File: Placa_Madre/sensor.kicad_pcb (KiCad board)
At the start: 2 copper layers, 10 parts, among them J1 Screw_Terminal_01x02, J2 Screw_Terminal_01x04, J3 Screw_Terminal_01x04, J4 Screw_Terminal_01x04, J5 Screw_Terminal_01x02, J6 Screw_Terminal_01x02, U1 RASPBERRY_PI_4B_4GB, U2 TMC2208_SILENTSTEPSTICK, U3 TMC2208_SILENTSTEPSTICK, U4 TMC2208_SILENTSTEPSTICK

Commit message: Add files via upload
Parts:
- J4: moved to B.Cu
- moved J1 78.1 mm to (58.4, 107.8), turned to 90 degrees
- moved J5 56.1 mm to (90.5, 110.5), turned to 90 degrees
- moved J6 43.7 mm to (120.0, 107.5), turned to 180 degrees
- moved J4 41.0 mm to (118.5, 99.5), turned to 90 degrees
- moved U4 38.6 mm to (133.3, 95.4)
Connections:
- U1 pad 11: unconnected-(U1-GPIO17/GPIO_GEN0-Pad11) -> DIR3
- U1 pad 12: STEP3 -> STEP2
- U1 pad 16: unconnected-(U1-GPIO23/GPIO_GEN4-Pad16) -> DIR2
- U1 pad 33: STEP2 -> STEP3
- U1 pad 35: DIR2 -> unconnected-(U1-GPIO19-Pad35)
- U1 pad 36: DIR -> DIR1
- U1 pad 38: DIR3 -> unconnected-(U1-GPIO20-Pad38)
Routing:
- net GND: track 0.00 -> 322.4 mm
- net VIO: track 0.00 -> 97.9 mm
- net STEP3: track 0.00 -> 93.2 mm
- net DIR3: track 0.00 -> 53.9 mm
- net STEP1: track 0.00 -> 20.8 mm
- net STEP2: track 0.00 -> 20.3 mm
- net VIO2: track 0.00 -> 18.1 mm
- net DIR1: track 0.00 -> 16.2 mm
- net VM2: track 0.00 -> 15.9 mm
- net DIR2: track 0.00 -> 15.7 mm
- net VM1: track 0.00 -> 13.7 mm
- net VM3: track 0.00 -> 10.3 mm
- net Net-(J3-Pin_4): track 0.00 -> 9.65 mm
- net Net-(J3-Pin_3): track 0.00 -> 9.65 mm
- net Net-(J3-Pin_2): track 0.00 -> 9.65 mm
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
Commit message: Add files via upload
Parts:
- added J7: Screw_Terminal_01x02, TerminalBlock_MetzConnect:TerminalBlock_MetzConnect_360272_1x01_Horizontal_ScrewM2.6, F.Cu at (67.5, 110.0)
- added J8: Screw_Terminal_01x02, TerminalBlock_MetzConnect:TerminalBlock_MetzConnect_360272_1x01_Horizontal_ScrewM2.6, F.Cu at (135.0, 107.5)
- added J9: Screw_Terminal_01x02, TerminalBlock_MetzConnect:TerminalBlock_MetzConnect_360272_1x01_Horizontal_ScrewM2.6, F.Cu at (137.5, 103.0)
- added REF**: TerminalBlock_MetzConnect_360272_1x01_Horizontal_ScrewM2.6, TerminalBlock_MetzConnect:TerminalBlock_MetzConnect_360272_1x01_Horizontal_ScrewM2.6, F.Cu at (107.5, 67.5)
- added REF**: TerminalBlock_MetzConnect_360272_1x01_Horizontal_ScrewM2.6, TerminalBlock_MetzConnect:TerminalBlock_MetzConnect_360272_1x01_Horizontal_ScrewM2.6, F.Cu at (107.5, 78.0)
- added REF**: TerminalBlock_MetzConnect_360272_1x01_Horizontal_ScrewM2.6, TerminalBlock_MetzConnect:TerminalBlock_MetzConnect_360272_1x01_Horizontal_ScrewM2.6, F.Cu at (144.5, 77.5)
- added REF**: TerminalBlock_MetzConnect_360272_1x01_Horizontal_ScrewM2.6, TerminalBlock_MetzConnect:TerminalBlock_MetzConnect_360272_1x01_Horizontal_ScrewM2.6, F.Cu at (120.0, 90.0)
- J1, J5, J6: footprint TerminalBlock_Phoenix:TerminalBlock_Phoenix_MPT-0,5-2-2.54_1x02_P2.54mm_Horizontal -> TerminalBlock_MetzConnect:TerminalBlock_MetzConnect_360272_1x01_Horizontal_ScrewM2.6
- J2, J3: value Screw_Terminal_01x04 -> Screw_Terminal_01x02; footprint TerminalBlock_Phoenix:TerminalBlock_Phoenix_MPT-0,5-4-2.54_1x04_P2.54mm_Horizontal -> TerminalBlock_MetzConnect:TerminalBlock_MetzConnect_360272_1x01_Horizontal_ScrewM2.6
- J4: value Screw_Terminal_01x04 -> Screw_Terminal_01x02; footprint TerminalBlock_Phoenix:TerminalBlock_Phoenix_MPT-0,5-4-2.54_1x04_P2.54mm_Horizontal -> TerminalBlock_MetzConnect:TerminalBlock_MetzConnect_360272_1x01_Horizontal_ScrewM2.6; moved to F.Cu
- moved J4 51.1 mm to (67.5, 103.0)
- moved J2 46.0 mm to (105.0, 105.0)
- moved J3 20.7 mm to (105.0, 112.5)
- moved J1 19.8 mm to (74.9, 118.8)
- moved J5 19.8 mm to (107.0, 121.5)
- moved J6 19.8 mm to (136.5, 118.5)
- moved U1 19.8 mm to (112.5, 57.5)
- moved U2 19.8 mm to (91.5, 106.0)
- moved U3 19.8 mm to (121.0, 107.2)
- moved U4 19.8 mm to (149.8, 106.4)
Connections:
- U1 pad 11: DIR3 -> unconnected-(U1-GPIO17/GPIO_GEN0-Pad11)
- U1 pad 12: STEP2 -> STEP3
- U1 pad 16: DIR2 -> unconnected-(U1-GPIO23/GPIO_GEN4-Pad16)
- U1 pad 33: STEP3 -> STEP2
- U1 pad 35: unconnected-(U1-GPIO19-Pad35) -> DIR2
- U1 pad 36: DIR1 -> DIR
- U1 pad 38: unconnected-(U1-GPIO20-Pad38) -> DIR3
- U2 pad JP2_3: Net-(J2-Pin_2) -> Net-(J7-Pin_2)
- U2 pad JP2_4: Net-(J2-Pin_1) -> Net-(J7-Pin_1)
- U2 pad JP2_5: Net-(J2-Pin_3) -> Net-(J4-Pin_1)
- U2 pad JP2_6: Net-(J2-Pin_4) -> Net-(J4-Pin_2)
- U3 pad JP2_5: Net-(J3-Pin_3) -> Net-(J2-Pin_1)
- U3 pad JP2_6: Net-(J3-Pin_4) -> Net-(J2-Pin_2)
- U4 pad JP2_3: Net-(J4-Pin_2) -> Net-(J8-Pin_2)
- U4 pad JP2_4: Net-(J4-Pin_1) -> Net-(J8-Pin_1)
- U4 pad JP2_5: Net-(J4-Pin_3) -> Net-(J9-Pin_1)
- U4 pad JP2_6: Net-(J4-Pin_4) -> Net-(J9-Pin_2)
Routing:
- net Net-(J7-Pin_2): track 0.00 -> 18.4 mm
- net Net-(J7-Pin_1): track 0.00 -> 18.2 mm
- net Net-(J4-Pin_2): track 8.62 -> 18.6 mm
- net GND: track 322.4 -> 312.5 mm
- net Net-(J4-Pin_1): track 8.62 -> 18.4 mm
- net Net-(J3-Pin_4): track 9.65 -> 0.00 mm
- net Net-(J3-Pin_3): track 9.65 -> 0.00 mm
- net Net-(J2-Pin_4): track 9.49 -> 0.00 mm
- net Net-(J2-Pin_3): track 9.49 -> 0.00 mm
- net Net-(J8-Pin_2): track 0.00 -> 9.05 mm
- net Net-(J8-Pin_1): track 0.00 -> 8.99 mm
- net Net-(J4-Pin_4): track 8.62 -> 0.00 mm
- net Net-(J4-Pin_3): track 8.62 -> 0.00 mm
- net Net-(J9-Pin_2): track 0.00 -> 7.49 mm
- net Net-(J9-Pin_1): track 0.00 -> 7.30 mm
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- added copper zone on B.Cu, net GND

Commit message: Add files via upload
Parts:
- removed the REF** at (107.5, 67.5)
- removed the REF** at (144.5, 77.5)
- moved REF** 16.2 mm to (123.5, 75.5), turned to 0 degrees
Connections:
- REF** pad 1: (no net) -> VIO (x2)
- U1 pad 13: unconnected-(U1-GPIO27/GPIO_GEN2-Pad13) -> STEP3
- U4 pad JP2_7: VIO2 -> VIO
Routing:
- net VIO: track 104.8 -> 144.5 mm
- net VIO2: track 18.1 -> 0.00 mm
- net STEP3: track 93.2 -> 80.5 mm
- net GND: track 312.5 -> 305.8 mm
- net DIR3: track 53.8 -> 60.1 mm
- net STEP2: track 25.2 -> 21.4 mm
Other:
- board outline added: 107 x 107.5 mm

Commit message: arreglando el pcb
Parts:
- removed J1, J2, J3, J4, J5, J6, J7, J8, J9: Screw_Terminal_01x02, TerminalBlock_MetzConnect:TerminalBlock_MetzConnect_360272_1x01_Horizontal_ScrewM2.6
- removed the REF** at (123.5, 75.5)
- removed the REF** at (120.0, 90.0)
- added REF**: TerminalBlock_MetzConnect_360291_1x01_Horizontal_ScrewM3.0_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, TerminalBlock_MetzConnect:TerminalBlock_MetzConnect_360291_1x01_Horizontal_ScrewM3.0_Boxed, F.Cu at (137.5, 107.5)
- added REF**: TerminalBlock_MetzConnect_360291_1x01_Horizontal_ScrewM3.0_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, TerminalBlock_MetzConnect:TerminalBlock_MetzConnect_360291_1x01_Horizontal_ScrewM3.0_Boxed, F.Cu at (140.0, 122.5)
- added REF**: TerminalBlock_MetzConnect_360291_1x01_Horizontal_ScrewM3.0_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, TerminalBlock_MetzConnect:TerminalBlock_MetzConnect_360291_1x01_Horizontal_ScrewM3.0_Boxed, F.Cu at (115.0, 125.0)
- added REF**: TerminalBlock_MetzConnect_360291_1x01_Horizontal_ScrewM3.0_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, TerminalBlock_MetzConnect:TerminalBlock_MetzConnect_360291_1x01_Horizontal_ScrewM3.0_Boxed, F.Cu at (105.0, 122.5)
- added REF**: TerminalBlock_MetzConnect_360291_1x01_Horizontal_ScrewM3.0_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, TerminalBlock_MetzConnect:TerminalBlock_MetzConnect_360291_1x01_Horizontal_ScrewM3.0_Boxed, F.Cu at (67.5, 115.0)
- added REF**: TerminalBlock_MetzConnect_360291_1x01_Horizontal_ScrewM3.0_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, TerminalBlock_MetzConnect:TerminalBlock_MetzConnect_360291_1x01_Horizontal_ScrewM3.0_Boxed, F.Cu at (141.5, 90.0)
- added REF**: TerminalBlock_MetzConnect_360291_1x01_Horizontal_ScrewM3.0_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, TerminalBlock_MetzConnect:TerminalBlock_MetzConnect_360291_1x01_Horizontal_ScrewM3.0_Boxed, F.Cu at (107.5, 107.5)
- added REF**: TerminalBlock_MetzConnect_360291_1x01_Horizontal_ScrewM3.0_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, TerminalBlock_MetzConnect:TerminalBlock_MetzConnect_360291_1x01_Horizontal_ScrewM3.0_Boxed, F.Cu at (125.0, 72.5)
- added REF**: TerminalBlock_MetzConnect_360291_1x01_Horizontal_ScrewM3.0_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, TerminalBlock_MetzConnect:TerminalBlock_MetzConnect_360291_1x01_Horizontal_ScrewM3.0_Boxed, F.Cu at (67.5, 102.5)
- added REF**: TerminalBlock_MetzConnect_360291_1x01_Horizontal_ScrewM3.0_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, TerminalBlock_MetzConnect:TerminalBlock_MetzConnect_360291_1x01_Horizontal_ScrewM3.0_Boxed, F.Cu at (122.5, 90.0)
- added REF**: TerminalBlock_MetzConnect_360291_1x01_Horizontal_ScrewM3.0_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, TerminalBlock_MetzConnect:TerminalBlock_MetzConnect_360291_1x01_Horizontal_ScrewM3.0_Boxed, F.Cu at (85.0, 125.0)
- added REF**: TerminalBlock_MetzConnect_360291_1x01_Horizontal_ScrewM3.0_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, TerminalBlock_MetzConnect:TerminalBlock_MetzConnect_360291_1x01_Horizontal_ScrewM3.0_Boxed, F.Cu at (155.0, 121.0)
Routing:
- net GND: track 305.8 -> 52.2 mm
- net VIO: track 144.5 -> 132.9 mm
- net VM2: track 15.9 -> 5.06 mm
- net Net-(J3-Pin_1): track 10.1 -> 19.7 mm
- net Net-(J8-Pin_1): track 8.99 -> 17.9 mm
- net unconnected-(U1-GPIO14/TXD0-Pad8): track 0.00 -> 7.76 mm
- net VM1: track 13.7 -> 6.17 mm
- net unconnected-(U1-GPIO15/RXD0-Pad10): track 0.00 -> 7.16 mm
- net Net-(J3-Pin_2): track 10.3 -> 15.5 mm
- net Net-(J9-Pin_2): track 7.49 -> 12.5 mm
- net Net-(J8-Pin_2): track 9.05 -> 13.7 mm
- net VM3: track 10.3 -> 13.9 mm
- net Net-(J2-Pin_2): track 10.2 -> 12.9 mm
- net Net-(J2-Pin_1): track 10.0 -> 7.80 mm
- net Net-(J7-Pin_2): track 18.4 -> 19.8 mm
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
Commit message: Correjir PPCB
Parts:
- moved REF** 21.7 mm to (99.0, 127.5)
- moved REF** 20.3 mm to (134.0, 127.5)
- moved REF** 7.91 mm to (122.5, 127.5), turned to 180 degrees
- moved REF** 7.07 mm to (145.0, 127.5)
- moved REF** 7.07 mm to (110.0, 127.5)
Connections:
- REF** pad 1: (no net) -> VIO
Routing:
- net Net-(J2-Pin_1): track 7.80 -> 28.1 mm
- net Net-(J2-Pin_2): track 12.9 -> 32.6 mm
- net Net-(J9-Pin_1): track 7.41 -> 26.3 mm
- net Net-(J9-Pin_2): track 12.5 -> 30.5 mm
- net VIO: track 132.9 -> 145.5 mm
- net VM2: track 5.06 -> 13.5 mm
- net Net-(J8-Pin_2): track 13.7 -> 19.3 mm
- net Net-(J8-Pin_1): track 17.9 -> 22.1 mm
- net Net-(J3-Pin_2): track 15.5 -> 18.4 mm
- net Net-(J3-Pin_1): track 19.7 -> 22.6 mm

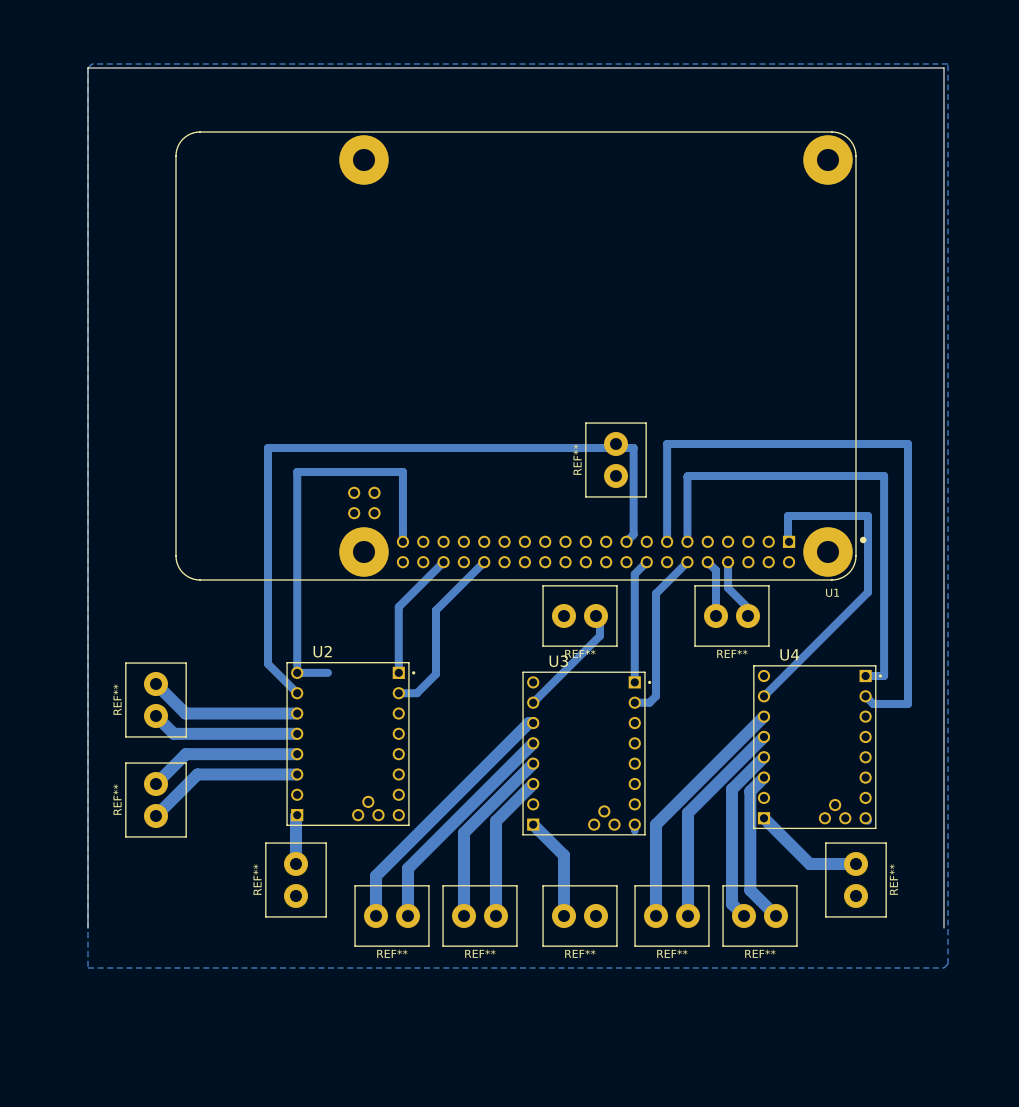
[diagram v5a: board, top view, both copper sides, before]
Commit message: Cambio de pi 4 a pi pico
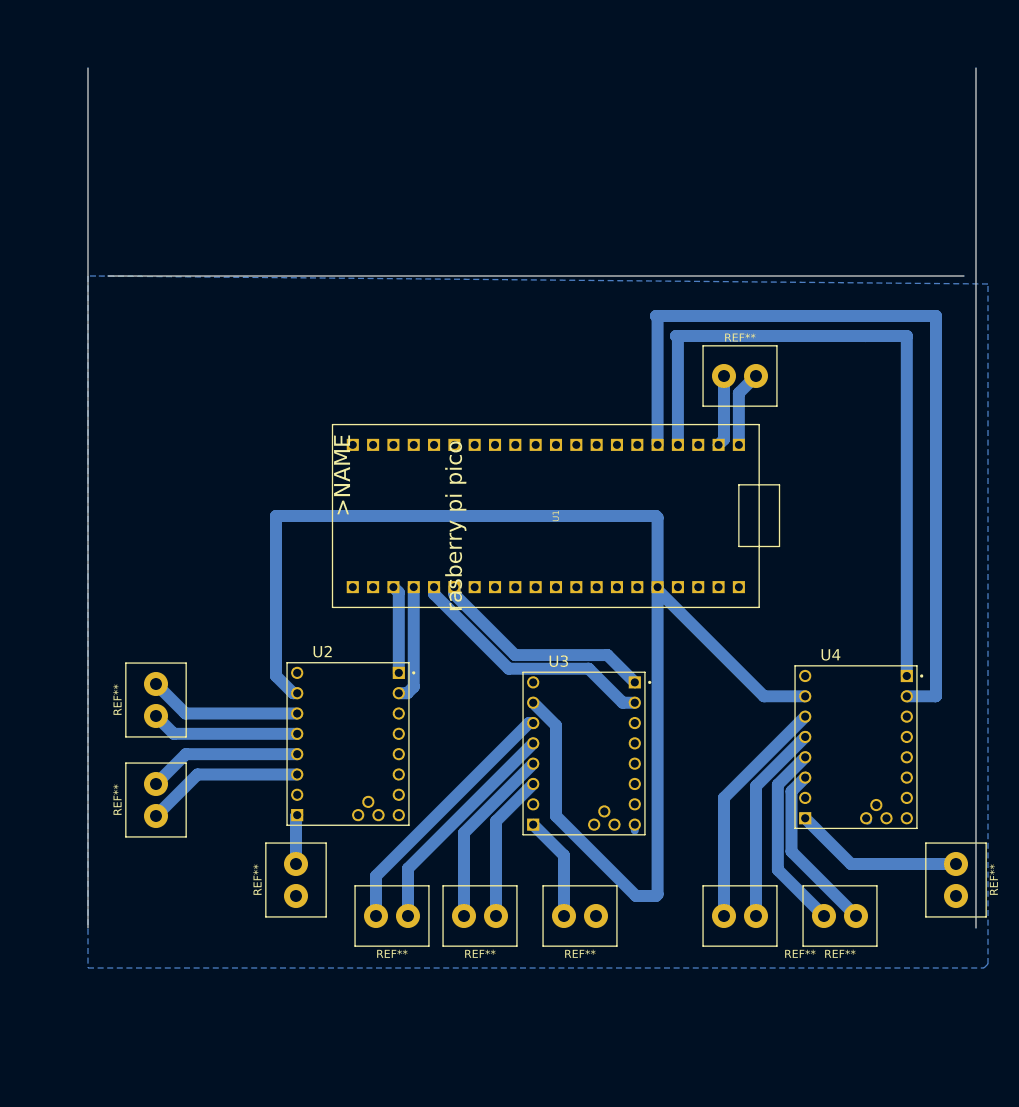
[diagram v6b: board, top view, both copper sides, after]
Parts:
- removed the REF** at (125.0, 72.5)
- removed the REF** at (122.5, 90.0)
- REF**: value TerminalBlock_MetzConnect_360291_1x01_Horizontal_ScrewM3.0_Boxed -> j10
- U1: value RASPBERRY_PI_4B_4GB -> RASPBERRY_PI_PICO; footprint pi 4:MODULE_RASPBERRY_PI_4B_4GB -> pi pico:RASPBERRY_PI_PICO
- moved REF** 30.1 mm to (138.5, 60.0), turned to 0 degrees
- moved U1 20.6 mm to (117.5, 77.5), turned to -90 degrees
- moved REF** 12.5 mm to (167.5, 121.0)
- moved REF** 10.0 mm to (155.0, 127.5)
- moved REF** 8.50 mm to (142.5, 127.5)
- moved U4 5.15 mm to (155.0, 106.4)
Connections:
- REF** pad 1: unconnected-(U1-GPIO15/RXD0-Pad10) -> Net-(J10-Pin_2)
- U2 pad JP1_1: DIR1 -> DIR
- U3 pad JP1_1: DIR2 -> STEP2
- U3 pad JP1_2: STEP2 -> DIR2
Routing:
- net GND: track 52.2 -> 0.84 mm
- net VIO: track 145.5 -> 175.0 mm
- net DIR3: track 60.1 -> 85.1 mm
- net STEP3: track 80.5 -> 102.4 mm
- net DIR1: track 16.2 -> 0.00 mm
- net DIR2: track 15.7 -> 31.6 mm
- net DIR: track 0.00 -> 11.0 mm
- net Net-(J10-Pin_2): track 0.00 -> 9.50 mm
- net Net-(J10-Pin_1): track 0.00 -> 8.89 mm
- net unconnected-(U1-GPIO14/TXD0-Pad8): track 7.76 -> 0.00 mm
- net STEP1: track 22.1 -> 14.7 mm
- net VM3: track 13.9 -> 21.2 mm
- net unconnected-(U1-GPIO15/RXD0-Pad10): track 7.16 -> 0.00 mm
- net STEP2: track 21.4 -> 28.0 mm
- net Net-(J8-Pin_2): track 19.3 -> 21.3 mm
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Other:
- board size 107 x 107.5 mm -> 111 x 107.5 mm
